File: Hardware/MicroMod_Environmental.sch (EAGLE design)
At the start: 34 parts, among them J1 MICROMOD_STANDARD, U1 SGP40, U2 EEPROM, U3 SHTC3, U4 3.3V, U5 STC31

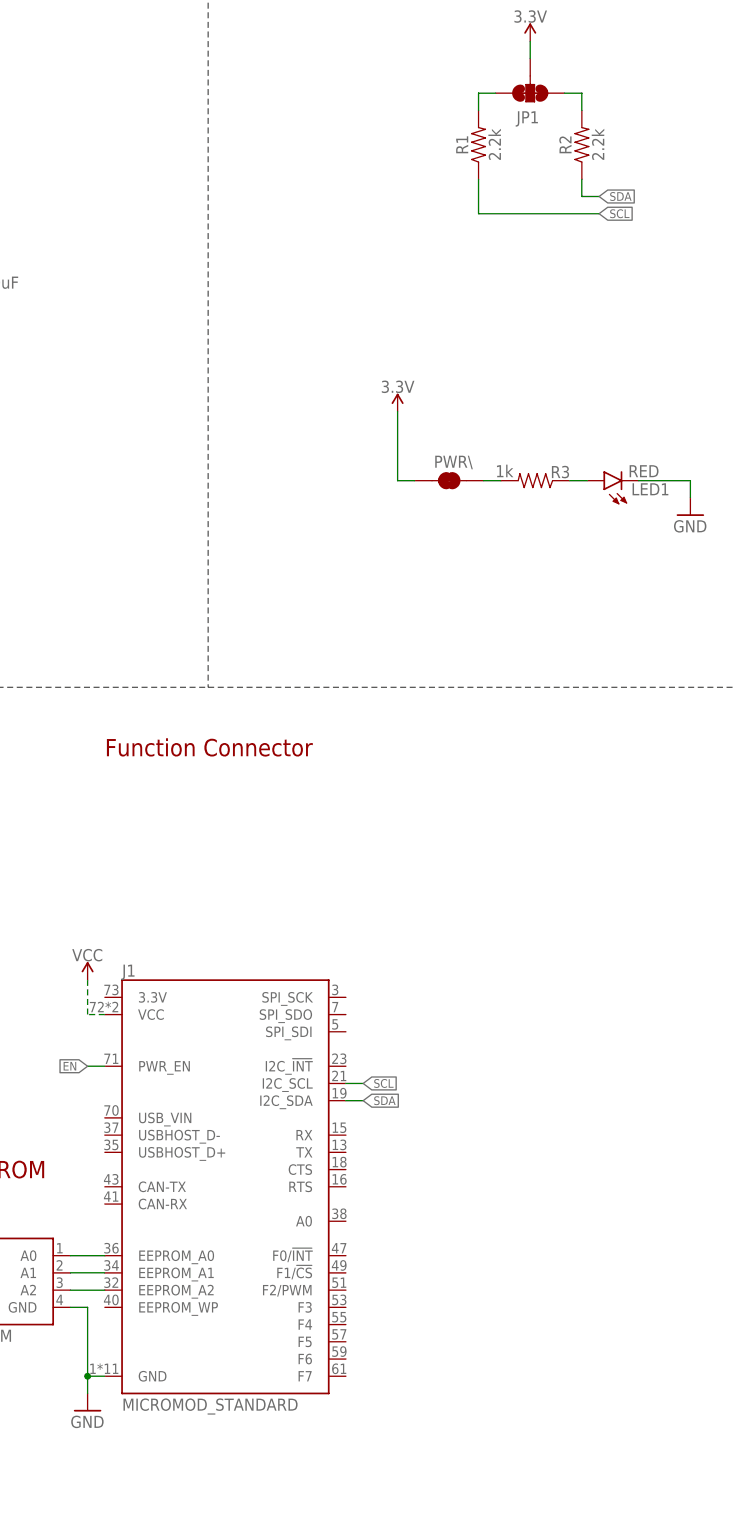
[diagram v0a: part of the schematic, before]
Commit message: Updates function board symbol to new one in the official SFE eagle library repo
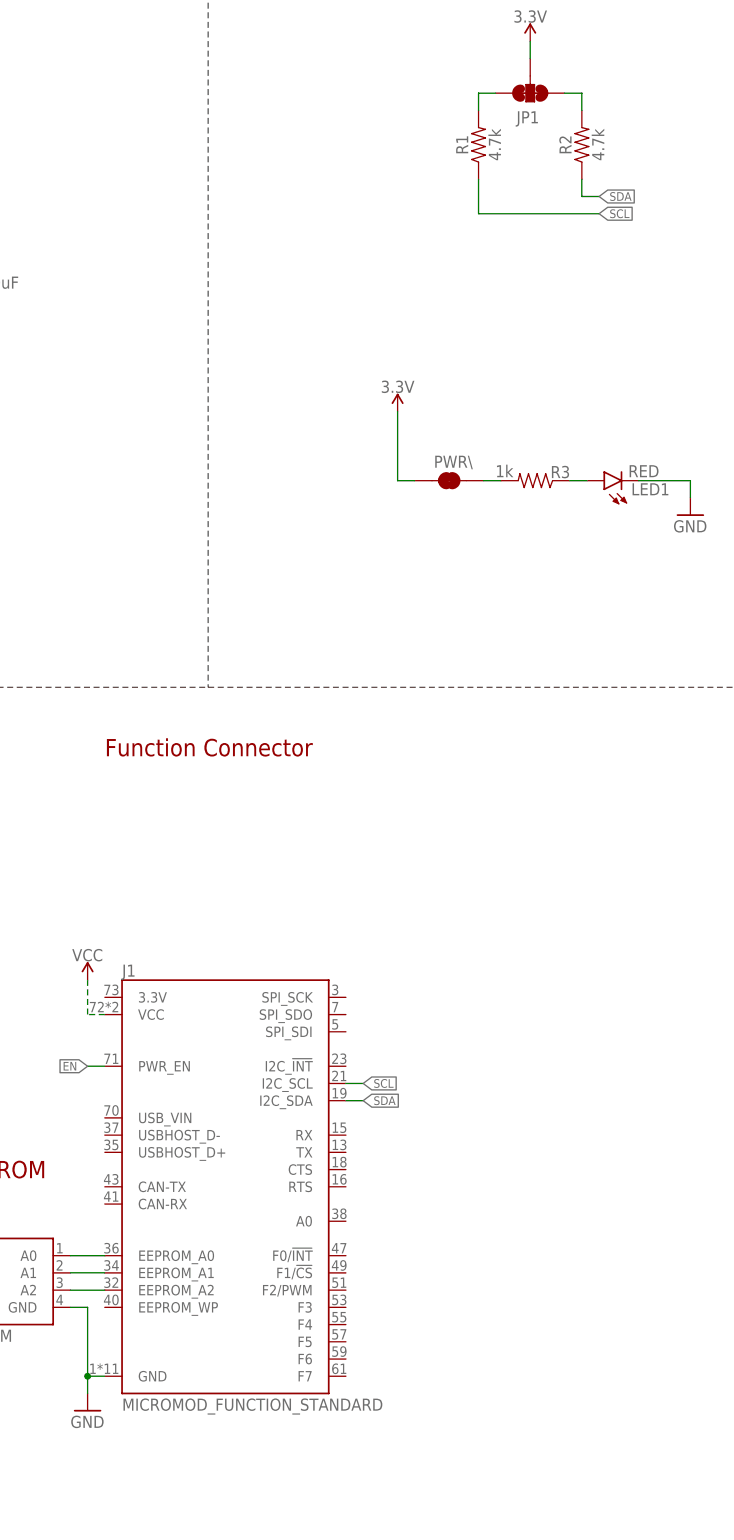
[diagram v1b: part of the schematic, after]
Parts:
- J1: value MICROMOD_STANDARD -> MICROMOD_FUNCTION_STANDARD; device SparkFun-MicroMod-Function:MICROMOD_STANDARD -> SparkFun-MicroMod:MICROMOD_FUNCTION_STANDARD
- R1, R2: value 2.2k -> 4.7k; device SparkFun-Resistors:2.2KOHM-0603-1/10W-1% -> SparkFun-Resistors:4.7KOHM-0603-1/10W-1%
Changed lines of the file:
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@@
 <?xml version="1.0" encoding="utf-8"?>
 <!DOCTYPE eagle SYSTEM "eagle.dtd">
-<eagle version="9.6.2">
+<eagle version="9.5.1">
 <drawing>
 <settings>
@@
 <parts>
 <part name="FRAME1" library="SparkFun-Aesthetics" deviceset="FRAME-LEDGER" device=""/>
-<part name="J1" library="SparkFun-MicroMod-Function" deviceset="MICROMOD" device="_STANDARD"/>
-<part name="R1" library="SparkFun-Resistors" deviceset="2.2KOHM" device="-0603-1/10W-1%" value="2.2k"/>
-<part name="R2" library="SparkFun-Resistors" deviceset="2.2KOHM" device="-0603-1/10W-1%" value="2.2k"/>
+<part name="J1" library="SparkFun-MicroMod" deviceset="MICROMOD_FUNCTION" device="_STANDARD"/>
+<part name="R1" library="SparkFun-Resistors" deviceset="4.7KOHM" device="-0603-1/10W-1%" value="4.7k"/>
+<part name="R2" library="SparkFun-Resistors" deviceset="4.7KOHM" device="-0603-1/10W-1%" value="4.7k"/>
 <part name="C5" library="SparkFun-Capacitors" deviceset="1.0UF" device="-0603-16V-10%" value="1.0uF"/>
 <part name="GND11" library="SparkFun-PowerSymbols" deviceset="GND" device=""/>
